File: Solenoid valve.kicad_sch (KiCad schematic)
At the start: 26 parts, among them J1 Conn_01x02, J2 Conn_01x02, J3 Conn_01x02, Q1 8050, Q2 CSD18540Q5B, U1 EL357N, U2 LM5060

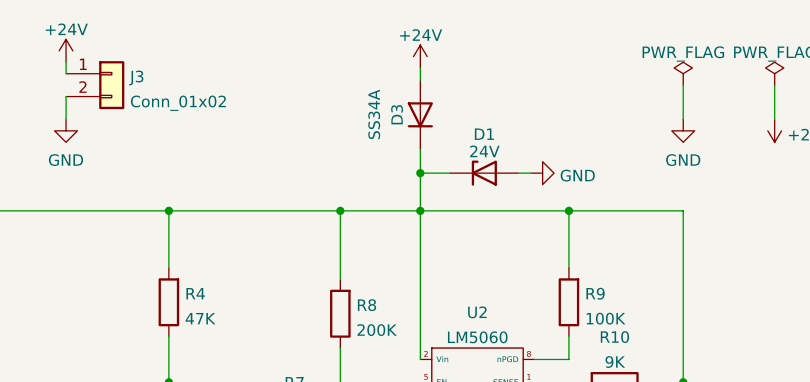
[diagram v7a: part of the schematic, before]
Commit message: Delete the input_diode
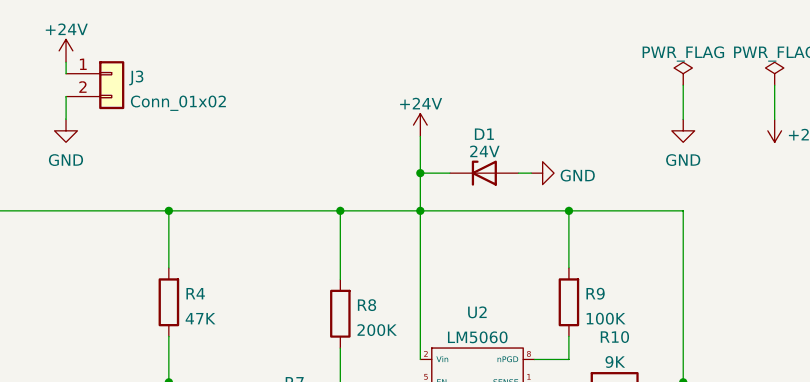
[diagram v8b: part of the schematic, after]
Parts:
- removed D3: SS34A, Diode_SMD:D_SMA, symbol Device:D
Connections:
- net +24V: now also D1.1 (K), Q2.5 (D), R1.2, R10.1, R4.2, R8.2, R9.2, U2.2 (Vin)
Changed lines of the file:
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@@
     (stroke (width 0) (type default))
   )
-  (wire (pts (xy 142.24 99.695) (xy 142.24 101.092))
+  (wire (pts (xy 142.24 107.315) (xy 142.24 111.379))
     (stroke (width 0) (type default))
   )
@@
   )
   (wire (pts (xy 87.63 144.78) (xy 99.06 144.78))
-    (stroke (width 0) (type default))
-  )
-  (wire (pts (xy 142.24 108.712) (xy 142.24 111.379))
     (stroke (width 0) (type default))
   )
@@
     )
   )
-  (symbol (lib_id "power:+24V") (at 142.24 99.695 0) (unit 1)
-    (in_bom yes) (on_board yes) (dnp no) (fields_autoplaced)
-    (property "Reference" "#PWR0101" (at 142.24 103.505 0)
-      (effects (font (size 1.27 1.27)) hide)
-    )
-    (property "Value" "+24V" (at 142.24 96.0905 0)
-      (effects (font (size 1.27 1.27)))
-    )
-    (property "Footprint" "" (at 142.24 99.695 0)
-      (effects (font (size 1.27 1.27)) hide)
-    )
-    (property "Datasheet" "" (at 142.24 99.695 0)
+  (symbol (lib_id "power:+24V") (at 142.24 107.315 0) (unit 1)
+    (in_bom yes) (on_board yes) (dnp no) (fields_autoplaced)
+    (property "Reference" "#PWR0101" (at 142.24 111.125 0)
+      (effects (font (size 1.27 1.27)) hide)
+    )
+    (property "Value" "+24V" (at 142.24 103.7105 0)
+      (effects (font (size 1.27 1.27)))
+    )
+    (property "Footprint" "" (at 142.24 107.315 0)
+      (effects (font (size 1.27 1.27)) hide)
+    )
+    (property "Datasheet" "" (at 142.24 107.315 0)
       (effects (font (size 1.27 1.27)) hide)
     )
@@
         )
       )
-    )
-  )
-  (symbol (lib_id "Device:D") (at 142.24 104.902 90) (unit 1)
-    (in_bom yes) (on_board yes) (dnp no)
-    (property "Reference" "D3" (at 139.7 104.902 0)
-      (effects (font (size 1.27 1.27)))
-    )
-    (property "Value" "SS34A" (at 137.16 104.902 0)
-      (effects (font (size 1.27 1.27)))
-    )
-    (property "Footprint" "Diode_SMD:D_SMA" (at 142.24 104.902 0)
-      (effects (font (size 1.27 1.27)) hide)
-    )
-    (property "Datasheet" "~" (at 142.24 104.902 0)
-      (effects (font (size 1.27 1.27)) hide)
-    )
-    (pin "1")
-    (pin "2")
-    (instances
-      (project "Solenoid valve"
-        (path "/e63e39d7-6ac0-4ffd-8aa3-1841a4541b55"
-          (reference "D3") (unit 1)
-        )
-      )
